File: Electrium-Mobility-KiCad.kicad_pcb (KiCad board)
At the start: 2 copper layers, 21 parts, among them J1 USB_C_Receptacle, Q1 BC817, Q2 BC817, U1 ESP32-WROOM-32E, U2 LCD-016N002L, U3 CH340C, U4 ESP32-WROOM-32, U5 MIC5504-3.3YM5

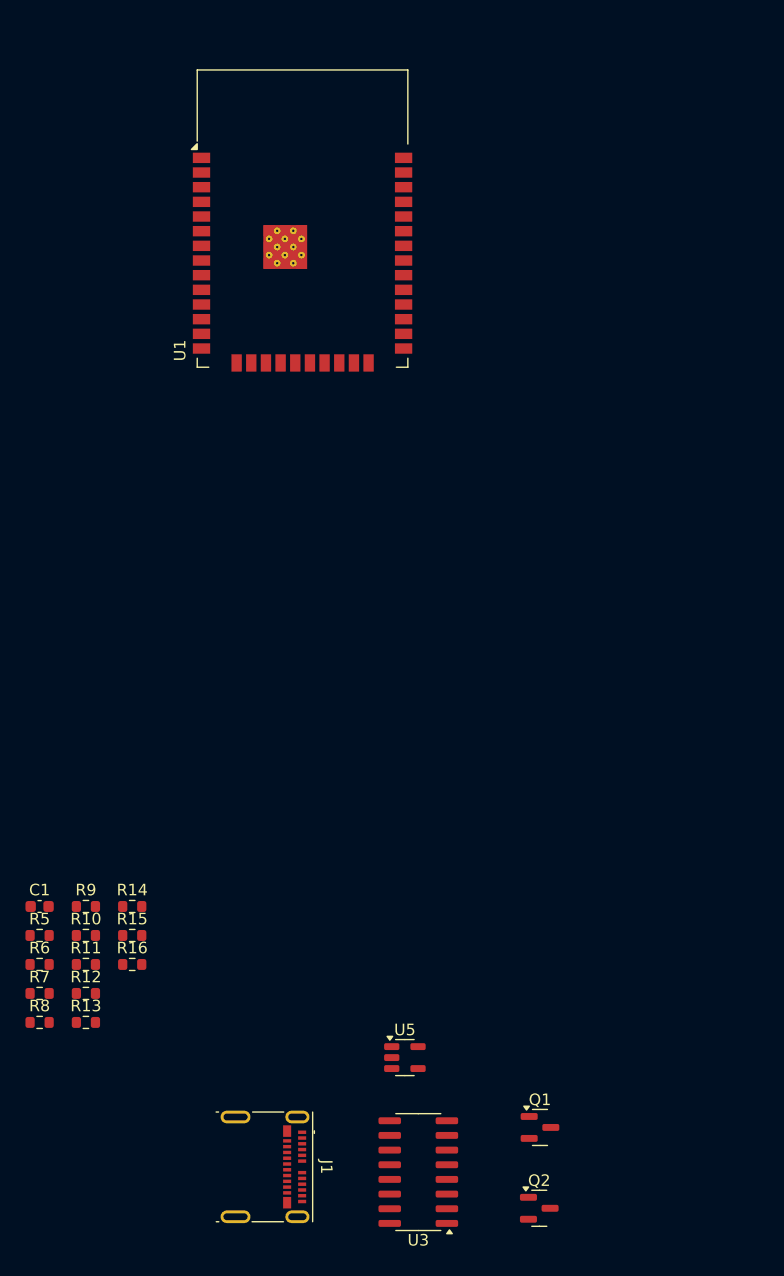
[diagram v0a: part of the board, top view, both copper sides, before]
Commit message: don't need pull down for RX and TX. Difficult to route D- and D+ with via's. Can you change line thickness?
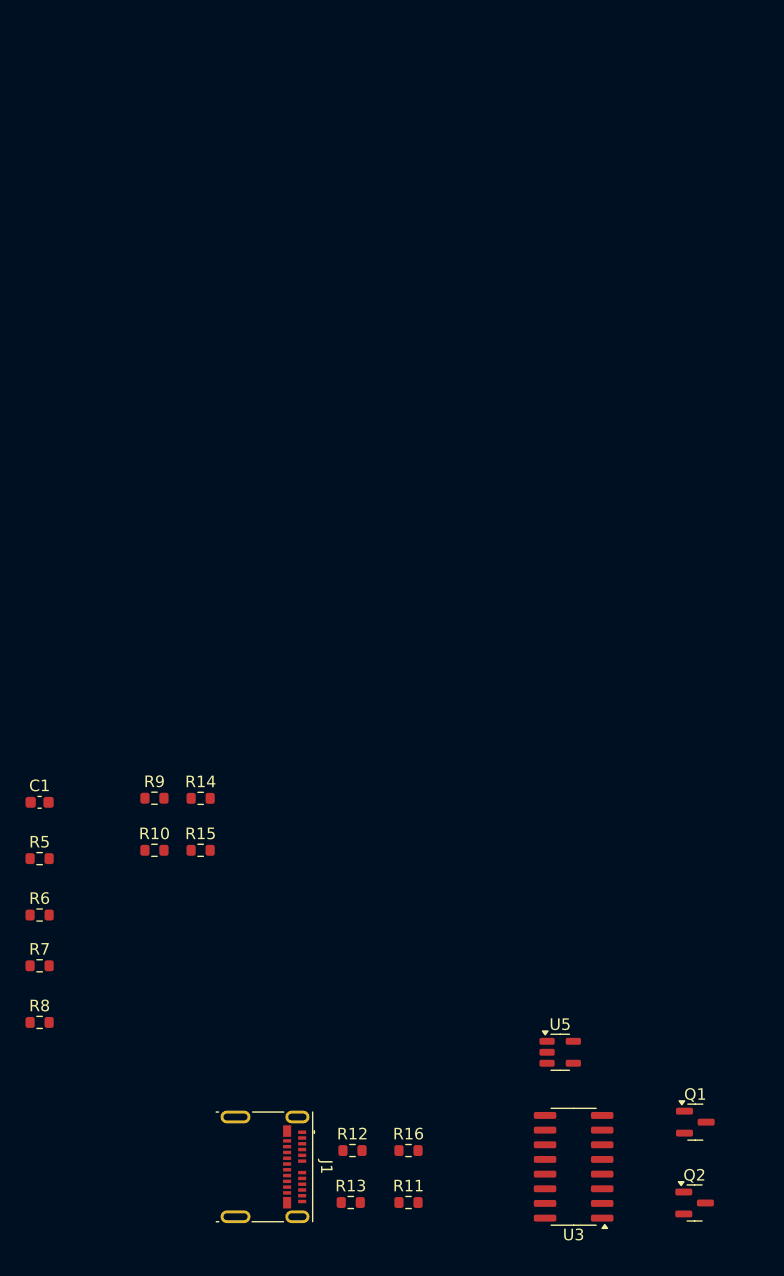
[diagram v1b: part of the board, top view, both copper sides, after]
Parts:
- removed U1: ESP32-WROOM-32E, RF_Module:ESP32-WROOM-32D
- moved R11 34.7 mm to (109.2, 186.0)
- moved R16 28.8 mm to (109.2, 181.5)
- moved R13 27.7 mm to (104.2, 186.0)
- moved R12 26.8 mm to (104.3, 181.5)
- moved U5 13.5 mm to (122.3, 173.0)
- moved Q1 13.5 mm to (134.0, 179.0)
- moved Q2 13.5 mm to (133.9, 186.0)
- moved U3 13.5 mm to (123.5, 182.9)
- moved R9 11.1 mm to (87.2, 151.0)
- moved R14 11.1 mm to (91.2, 151.0)
- moved R10 9.47 mm to (87.2, 155.5)
- moved R15 9.46 mm to (91.2, 155.5)
- moved C1 9.02 mm to (77.2, 151.3)
- moved R5 6.66 mm to (77.2, 156.2)
- moved R6 4.28 mm to (77.2, 161.1)
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
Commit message: saved file again and committing to be sure
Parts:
- U4: moved to B.Cu
- moved R9 76.3 mm to (158.7, 177.4), turned to 90 degrees
- moved R10 70.8 mm to (155.7, 173.0), turned to 90 degrees
- moved R15 60.9 mm to (149.7, 172.4), turned to 90 degrees
- moved R14 59.5 mm to (146.2, 173.5), turned to 90 degrees
- moved J1 56.0 mm to (152.7, 186.0), turned to 0 degrees
- moved R12 55.1 mm to (158.7, 172.9), turned to 90 degrees
- moved R11 47.4 mm to (155.7, 177.4), turned to 90 degrees
- moved R13 45.6 mm to (148.7, 176.5), turned to 90 degrees
- moved R16 42.4 mm to (149.7, 169.0), turned to 90 degrees
- moved U3 34.5 mm to (150.7, 161.7), turned to 90 degrees
- moved Q2 34.4 mm to (163.6, 168.6), turned to 180 degrees
- moved Q1 29.8 mm to (163.6, 175.6), turned to 180 degrees
- moved U4 26.0 mm to (153.6, 145.3), turned to 90 degrees
- moved U5 24.0 mm to (142.7, 160.4), turned to 90 degrees
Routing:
- net GND: track 0.00 -> 6.44 mm, vias 0 -> 4
- net /USB and Programmer/USB_D-: track 0.00 -> 5.32 mm, vias 0 -> 1
- net /USB and Programmer/USB_D+: track 0.00 -> 2.29 mm, vias 0 -> 2

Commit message: i saved and close pcb layout, hopefully saved properly
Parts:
- removed R10, R11, R12, R13, R14, R15, R16, R9: 47k, Resistor_SMD:R_0603_1608Metric
- moved R8 78.6 mm to (155.5, 178.0), turned to -90 degrees
- moved R7 73.0 mm to (149.0, 178.7), turned to -90 degrees
- moved C1 58.9 mm to (134.7, 164.3)
- moved R5 58.9 mm to (134.7, 169.2)
- moved R6 58.9 mm to (134.7, 174.1)
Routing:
- net /USB and Programmer/USB_D-: track 5.32 -> 20.6 mm, vias 1 -> 3
- net +5V: track 0.00 -> 12.5 mm, vias 0 -> 2
- net Net-(J1-CC1): track 0.00 -> 8.86 mm, vias 0 -> 2
- net /USB and Programmer/USB_D+: track 2.29 -> 1.66 mm, vias 2 -> 0
- net GND: track 6.44 -> 6.98 mm

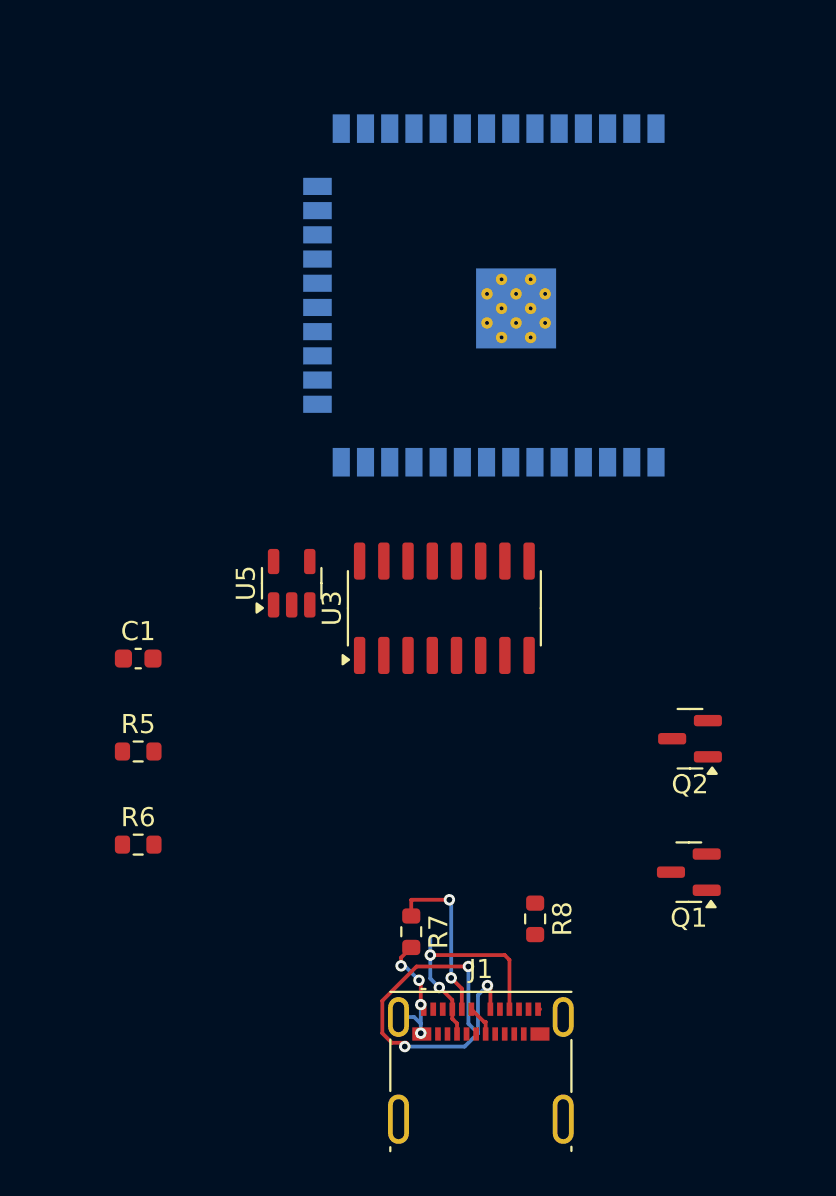
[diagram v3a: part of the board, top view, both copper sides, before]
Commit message: check connectivity for the ones I couldn't route, i think they're impossible
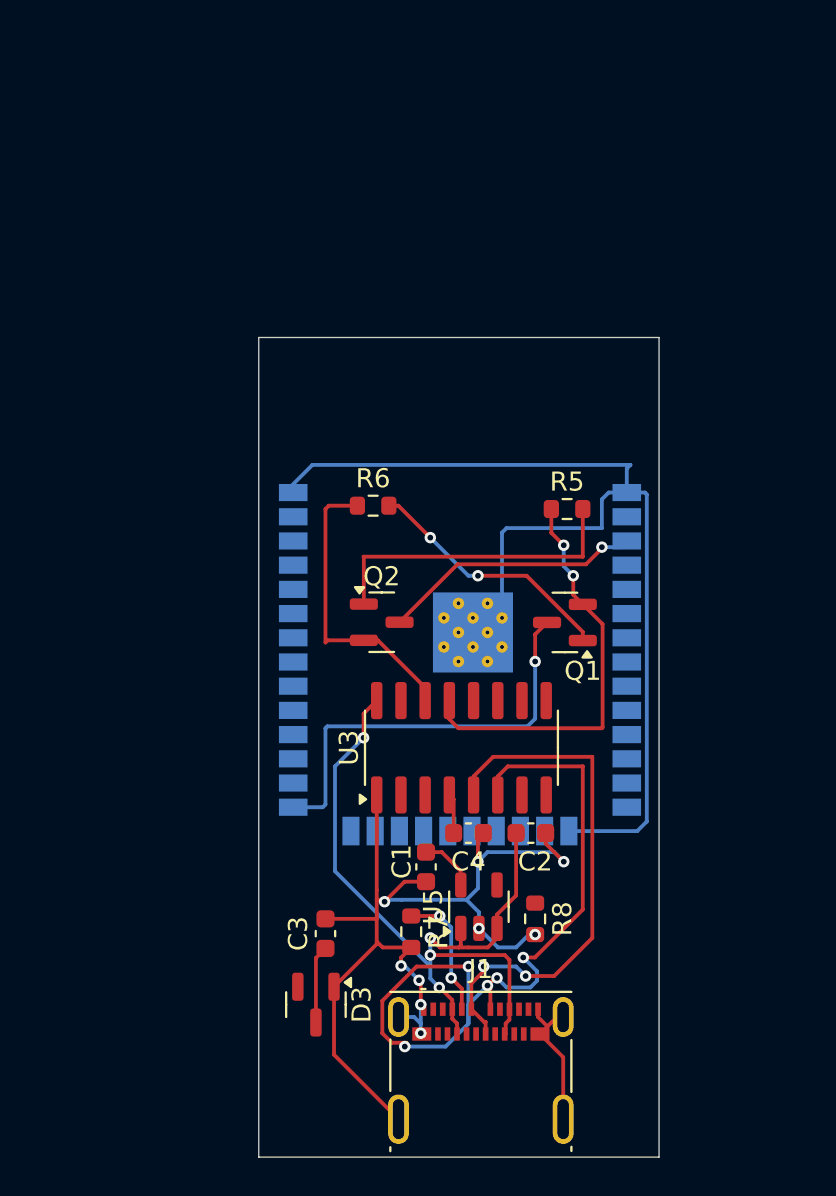
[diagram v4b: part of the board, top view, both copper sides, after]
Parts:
- added C2: 100nF, Capacitor_SMD:C_0603_1608Metric, F.Cu at (155.3, 173.5)
- added C3: 100nF, Capacitor_SMD:C_0603_1608Metric, F.Cu at (144.5, 178.8)
- added C4: 100nF, Capacitor_SMD:C_0603_1608Metric, F.Cu at (152.0, 173.5)
- added D3: D_Zener, Package_TO_SOT_SMD:SOT-23, F.Cu at (144.0, 182.5)
- moved R5 25.8 mm to (157.2, 156.5)
- moved R6 21.6 mm to (147.0, 156.3)
- moved U5 19.6 mm to (152.6, 177.4)
- moved U4 18.7 mm to (151.6, 163.9), turned to 180 degrees
- moved C1 18.6 mm to (149.8, 175.3), turned to -90 degrees
- moved Q2 17.3 mm to (147.4, 162.4), turned to 0 degrees
- moved Q1 14.6 mm to (157.1, 162.4)
- moved U3 7.37 mm to (151.6, 169.0)
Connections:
- J1 pad A10: Net-(J1-RX2-) -> unconnected-(J1-RX2--PadA10)
- J1 pad A11: Net-(J1-RX2+) -> unconnected-(J1-RX2+-PadA11)
- J1 pad A2: Net-(J1-TX1+) -> unconnected-(J1-TX1+-PadA2)
- J1 pad A3: Net-(J1-TX1-) -> unconnected-(J1-TX1--PadA3)
- J1 pad B10: Net-(J1-RX1-) -> unconnected-(J1-RX1--PadB10)
- J1 pad B11: Net-(J1-RX1+) -> unconnected-(J1-RX1+-PadB11)
- J1 pad B2: Net-(J1-TX2+) -> unconnected-(J1-TX2+-PadB2)
- J1 pad B3: Net-(J1-TX2-) -> unconnected-(J1-TX2--PadB3)
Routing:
- net Net-(U4-GND-Pad1): track 0.00 -> 55.1 mm
- net GND: track 6.98 -> 61.6 mm, vias 4 -> 9
- net +5V: track 12.5 -> 46.1 mm, vias 2 -> 4
- net /USB and Programmer/USB_D+: track 1.66 -> 28.0 mm, vias 0 -> 2
- net /USB and Programmer/ESP_IO0: track 0.00 -> 22.3 mm, vias 0 -> 1
- net Net-(Q1-E): track 0.00 -> 21.8 mm, vias 0 -> 2
- net /USB and Programmer/USB_D-: track 20.6 -> 41.3 mm, vias 3 -> 5
- net Net-(Q2-B): track 0.00 -> 16.5 mm
- net Net-(Q2-E): track 0.00 -> 15.7 mm
- net /USB and Programmer/ESP_EN: track 0.00 -> 13.7 mm, vias 0 -> 1
- net Net-(Q1-B): track 0.00 -> 13.4 mm, vias 0 -> 2
- net +3.3V: track 0.00 -> 2.24 mm
- net Net-(U3-V3): track 0.00 -> 2.09 mm
- net Net-(J1-CC1): track 8.86 -> 6.87 mm
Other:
- board outline added: 21 x 43 mm

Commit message: This sbould be the final pcb layout, adjust pcb size and delete random lcd on there?
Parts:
- C1: moved to B.Cu
- moved C2 11.3 mm to (145.4, 167.9), turned to 90 degrees
- moved C1 4.62 mm to (153.8, 177.5), turned to 0 degrees
- moved R6 4.28 mm to (146.8, 160.6)
- moved R5 4.11 mm to (156.9, 160.6)
- moved C4 3.32 mm to (150.8, 176.6), turned to -90 degrees
- moved R8 3.10 mm to (157.3, 180.5), turned to 0 degrees
- moved Q1 2.31 mm to (156.9, 164.8)
- moved Q2 2.31 mm to (147.3, 164.7)
- moved U3 2.31 mm to (151.4, 171.3)
- moved U4 2.31 mm to (151.4, 166.2)
- moved R7 2.23 mm to (150.3, 180.5), turned to 180 degrees
- moved U5 1.43 mm to (153.9, 177.7)
- moved C3 1.34 mm to (145.7, 179.4)
- moved D3 1.34 mm to (145.2, 183.1)
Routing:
- net GND: track 61.6 -> 0.58 mm, vias 9 -> 0
- net Net-(U4-GND-Pad1): track 55.1 -> 0.32 mm
- net /USB and Programmer/USB_D-: track 41.3 -> 15.6 mm, vias 5 -> 3
- net +5V: track 46.1 -> 25.1 mm, vias 4 -> 2
- net /USB and Programmer/ESP_TX: track 0.00 -> 20.1 mm, vias 0 -> 1
- net /USB and Programmer/USB_D+: track 28.0 -> 12.0 mm, vias 2 -> 0
- net /USB and Programmer/ESP_RX: track 0.00 -> 15.7 mm, vias 0 -> 3
- net Net-(J1-CC2): track 0.00 -> 5.29 mm, vias 0 -> 2
- net Net-(J1-CC1): track 6.87 -> 2.47 mm, vias 2 -> 0
- net Net-(Q2-E): track 15.7 -> 11.5 mm
- net /USB and Programmer/ESP_IO0: track 22.3 -> 18.3 mm
- net Net-(Q2-B): track 16.5 -> 13.6 mm, vias 0 -> 2
- net Net-(Q1-E): track 21.8 -> 19.8 mm
- net +3.3V: track 2.24 -> 2.85 mm, vias 0 -> 1
- added copper zone on B.Cu, net GND
- added copper zone on F.Cu, net GND

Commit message: final sizing
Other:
- board size 21 x 43 mm -> 21.1 x 40.6 mm
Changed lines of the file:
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@@
 		(tags "resistor")
 		(property "Reference" "R7"
-			(at -0.1 1.3 360)
+			(at -0.1 1.3 0)
 			(layer "F.SilkS")
 			(effects
@@
 		)
 		(property "Value" "5.1k"
-			(at 0 1.43 360)
+			(at 0 1.43 0)
 			(layer "F.Fab")
 			(hide yes)
@@
 		)
 		(fp_text user "${REFERENCE}"
-			(at 0 0 360)
+			(at 0 0 0)
 			(layer "F.Fab")
 			(effects
@@
 		(tags "resistor")
 		(property "Reference" "R8"
-			(at 0 -1.325 360)
+			(at 0 -1.325 0)
 			(layer "F.SilkS")
 			(effects
@@
 		)
 		(property "Value" "5.1k"
-			(at 0 1.43 360)
+			(at 0 1.43 0)
 			(layer "F.Fab")
 			(hide yes)
@@
 		)
 		(fp_text user "${REFERENCE}"
-			(at 0 0 360)
+			(at 0 0 0)
 			(layer "F.Fab")
 			(effects
@@
 		(tags "capacitor")
 		(property "Reference" "C1"
-			(at -0.275 -1.275 0)
+			(at 0.075 1.4 0)
 			(layer "B.SilkS")
 			(effects
@@
 	)
 	(gr_rect
-		(start 141 147.5)
-		(end 162 190.5)
+		(start 140.8 149.8)
+		(end 161.9 190.4)
 		(stroke
 			(width 0.05)

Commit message: the part tags are gone? opened incorrectly?
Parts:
- moved C2 0.07 mm to (145.4, 168.0)
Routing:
- net +5V: track 25.1 -> 41.5 mm, vias 2 -> 4
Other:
- board size 21.1 x 40.6 mm -> 21 x 41 mm
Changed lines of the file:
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@@
 	(footprint "Capacitor_SMD:C_0603_1608Metric"
 		(layer "F.Cu")
-		(at 145.4125 167.905 90)
+		(at 145.4125 167.975 90)
 		(descr "Capacitor SMD 0603 (1608 Metric), square (rectangular) end terminal, IPC_7351 nominal, (Body size source: IPC-SM-782 page 76, https://www.pcb-3d.com/wordpress/wp-content/uploads/ipc-sm-782a_amendment_1_and_2.pdf), generated with kicad-footprint-generator")
 		(tags "capacitor")
@@
 		(tags "Single 2.4 GHz Wi-Fi and Bluetooth combo  chip")
 		(property "Reference" "U4"
-			(at -10.61 -8.43 90)
+			(at 2.67 -11.31 180)
 			(layer "B.SilkS")
 			(effects
@@
 	)
 	(gr_rect
-		(start 140.8 149.8)
-		(end 161.9 190.4)
+		(start 140.95 149.5)
+		(end 161.95 190.5)
 		(stroke
 			(width 0.05)
@@
 	)
 	(segment
+		(start 145.8575 170)
+		(end 147.0025 168.855)
+		(width 0.2)
+		(layer "F.Cu")
+		(net 3)
+	)
+	(segment
+		(start 144.4 178.85)
+		(end 145.7 180.15)
+		(width 0.2)
+		(layer "F.Cu")
+		(net 3)
+	)
+	(segment
 		(start 151.1525 182.74)
 		(end 151.1525 181.625)
@@
 	)
 	(segment
+		(start 146.8475 168.7)
+		(end 147.0025 168.855)
+		(width 0.2)
+		(layer "F.Cu")
+		(net 3)
+	)
+	(segment
+		(start 154.9 178.8)
+		(end 154.9 179.153052)
+		(width 0.2)
+		(layer "F.Cu")
+		(net 3)
+	)
+	(segment
+		(start 144.4 173.8)
+		(end 144.4 178.85)
+		(width 0.2)
+		(layer "F.Cu")
+		(net 3)
+	)
+	(segment
+		(start 153 179.153052)
+		(end 153 178.8)
+		(width 0.2)
+		(layer "F.Cu")
+		(net 3)
+	)
+	(segment
 		(start 154.1525 183.24)
 		(end 154.1525 182.74)
@@
 	)
 	(segment
-		(start 145.4125 168.68)
-		(end 146.8275 168.68)
+		(start 145.4 170)
+		(end 145.8575 170)
 		(width 0.2)
 		(layer "F.Cu")
@@
 	)
 	(segment
-		(start 151.4025 184.64)
-		(end 151.4025 184.04)
+		(start 145.2 184.0375)
+		(end 146.0625 184.9)
+		(width 0.2)
+		(layer "F.Cu")
+		(net 3)
+	)
+	(segment
+		(start 145.4325 168.7)
+		(end 146.8475 168.7)
 		(width 0.2)
 		(layer "F.Cu")
@@
 	)
 	(segment
+		(start 146.0625 184.9)
+		(end 151.1425 184.9)
+		(width 0.2)
+		(layer "F.Cu")
+		(net 3)
+	)
+	(segment
 		(start 151.4025 183.59)
 		(end 151.4025 184.04)
@@
 	)
 	(segment
-		(start 151.3525 184.69)
-		(end 151.4025 184.64)
+		(start 154.290552 179.7625)
+		(end 153.609448 179.7625)
 		(width 0.2)
 		(layer "F.Cu")
@@
 	)
 	(segment
-		(start 146.8275 168.68)
-		(end 147.0025 168.855)
+		(start 151.4025 184.64)
+		(end 151.4025 184.04)
 		(width 0.2)
 		(layer "F.Cu")
@@
 	)
 	(segment
-		(start 145.8525 184.69)
-		(end 151.3525 184.69)
+		(start 153.609448 179.7625)
+		(end 153 179.153052)
 		(width 0.2)
 		(layer "F.Cu")
@@
 	)
 	(segment
+		(start 145.4125 168.68)
+		(end 145.4325 168.7)
+		(width 0.2)
+		(layer "F.Cu")
+		(net 3)
+	)
+	(segment
 		(start 154.1525 182.74)
 		(end 154.1525 181.9475)
@@
 	)
 	(segment
-		(start 145.2 184.0375)
-		(end 145.8525 184.69)
+		(start 154.9 179.153052)
+		(end 154.290552 179.7625)
+		(width 0.2)
+		(layer "F.Cu")
+		(net 3)
+	)
+	(segment
+		(start 151.1425 184.9)
+		(end 151.4025 184.64)
 		(width 0.2)
 		(layer "F.Cu")
@@
 	)
 	(via
+		(at 144.4 173.8)
+		(size 0.6)
+		(drill 0.3)
+		(layers "F.Cu" "B.Cu")
+		(net 3)
+	)
+	(via
+		(at 145.4 170)
+		(size 0.6)
+		(drill 0.3)
+		(layers "F.Cu" "B.Cu")
+		(net 3)
+	)
+	(via
 		(at 151.1775 181.6)
 		(size 0.35)
@@
 	)
 	(segment
+		(start 145.4 172.8)
+		(end 144.4 173.8)
+		(width 0.2)
+		(layer "B.Cu")
+		(net 3)
+	)
+	(segment
 		(start 153 180.1)
 		(end 153 179.8)
@@
 	)
 	(segment
+		(start 145.4 170)
+		(end 145.4 172.8)
+		(width 0.2)
+		(layer "B.Cu")
+		(net 3)
+	)
+	(segment
 		(start 151.5 181.6)
 		(end 153 180.1)
@@
 		(drill 0.2)
 		(layers "F.Cu" "B.Cu")
+		(teardrops
+			(best_length_ratio 0.5)
+			(max_length 1)
+			(best_width_ratio 1)
+			(max_width 2)
+			(curve_points 0)
+			(filter_ratio 0.9)
+			(enabled yes)
+			(allow_two_segments yes)
+			(prefer_zone_connections yes)
+		)
 		(net 7)
 	)
@@
 	)
 	(zone
+		(net 7)
+		(net_name "/USB and Programmer/USB_D-")
+		(layer "F.Cu")
+		(name "$teardrop_padvia$")
+		(hatch full 0.1)
+		(priority 30000)
+		(attr
+			(teardrop
+				(type padvia)
+			)
+		)
+		(connect_pads yes
+			(clearance 0)
+		)
+		(min_thickness 0.0254)
+		(filled_areas_thickness no)
+		(fill yes
+			(thermal_gap 0.5)
+			(thermal_bridge_width 0.5)
+			(island_removal_mode 1)
+			(island_area_min 10)
+		)
+		(polygon
+			(pts
+				(xy 155.693198 179.92135) (xy 155.551777 179.779929) (xy 155.30803 179.936448) (xy 155.374293 180.098834)
+				(xy 155.536679 180.165097)
+			)
+		)
+	)
+	(zone
 		(net 1)
 		(net_name "GND")
@@
 		(polygon
 			(pts
-				(xy 140.8125 157.805) (xy 161.8125 157.805) (xy 161.8125 192.805) (xy 140.8125 192.805)
+				(xy 141.0125 156.8) (xy 162.0125 156.8) (xy 162.0125 190.5) (xy 141.0125 190.5)
+			)
+		)
+	)
+	(zone
+		(net 7)
+		(net_name "/USB and Programmer/USB_D-")
+		(layer "B.Cu")
+		(name "$teardrop_padvia$")
+		(hatch full 0.1)
+		(priority 30000)
+		(attr
+			(teardrop
+				(type padvia)
+			)
+		)
+		(connect_pads yes
+			(clearance 0)
+		)
+		(min_thickness 0.0254)
+		(filled_areas_thickness no)
+		(fill yes
+			(thermal_gap 0.5)
+			(thermal_bridge_width 0.5)
+			(island_removal_mode 1)
+			(island_area_min 10)
+		)
+		(polygon
+			(pts
+				(xy 155.072911 180.285668) (xy 155.214332 180.427089) (xy 155.498744 180.221871) (xy 155.375707 180.09742)
+				(xy 155.213321 180.031157)
 			)
 		)
